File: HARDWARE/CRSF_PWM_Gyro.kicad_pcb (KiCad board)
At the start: 4 copper layers, 32.5 x 22 mm, 27 parts, among them J1 USB_C_Receptacle_USB2.0_16P, J2 Conn_01x21, SW1 SW_SPST, U1 TCR2EF33_LMCT, U2 STM32G431KBTx, Y1 Crystal_GND24

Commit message: Clean up routing and layout
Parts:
- moved C12 2.01 mm to (130.2, 82.6), turned to 0 degrees
- moved R3 2.01 mm to (130.2, 83.8), turned to 180 degrees
- moved R1 1.93 mm to (143.5, 98.3)
- moved R2 1.93 mm to (143.5, 97.1)
- moved R5 1.10 mm to (149.8, 83.1)
- moved C4 0.90 mm to (144.3, 78.7)
- moved LED1 0.40 mm to (147.5, 96.2)
- moved R4 0.30 mm to (150.5, 96.2)
- moved C10 0.10 mm to (130.2, 84.9)
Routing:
- net GND: track 10.1 -> 23.8 mm, vias 26 -> 24
- net Net-(SW1-A): track 15.2 -> 26.9 mm
- net CH4_PWM: track 10.4 -> 7.67 mm
- net +3.3V: track 21.3 -> 23.9 mm, vias 10 -> 9
- net CH3_PWM: track 10.2 -> 7.61 mm
- net CH5_PWM: track 10.9 -> 8.39 mm
- net N_RESET: track 20.7 -> 23.2 mm, vias 2 -> 3
- net CH6_PWM: track 13.1 -> 10.7 mm
- net V_ESC: track 7.83 -> 5.46 mm
- net Net-(J1-CC2): track 23.5 -> 21.5 mm
- net Net-(J1-CC1): track 22.5 -> 20.5 mm
- net Net-(D1-A-Pad2): track 36.4 -> 38.2 mm
- net CH2_PWM: track 13.4 -> 15.2 mm
- net Net-(MT1-AP_SDA/AP_SDIO/AP_SDI): track 10.6 -> 11.9 mm
- net Net-(MT1-AP_SDO/AP_AD0): track 7.95 -> 9.17 mm
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
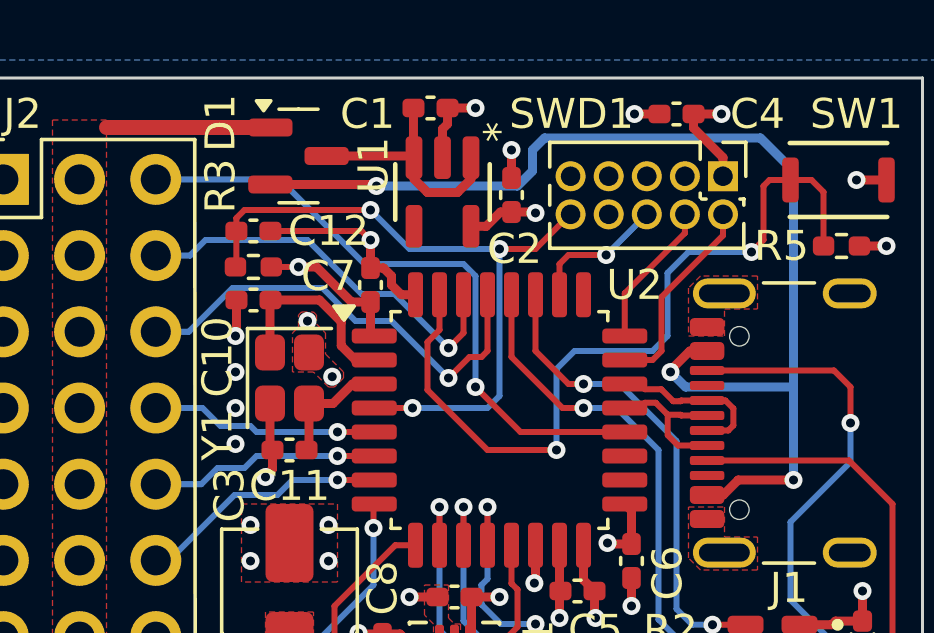
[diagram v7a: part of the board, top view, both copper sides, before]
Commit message: Move some silkscreen text
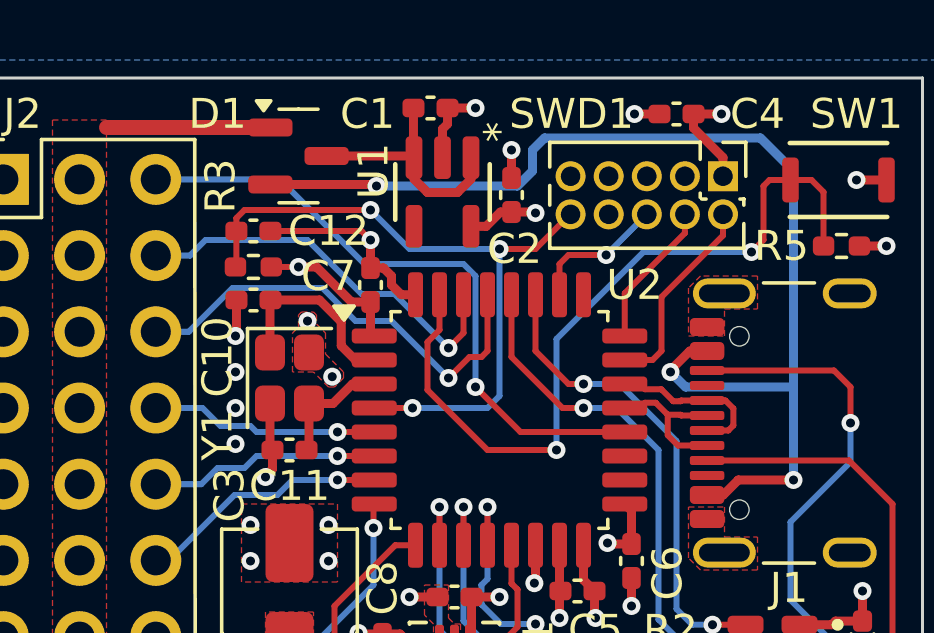
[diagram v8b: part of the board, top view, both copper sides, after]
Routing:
- net Net-(SW1-A): track 26.9 -> 26.3 mm
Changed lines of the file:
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@@
 		(tags "TCR2EF33_LMCT ")
 		(property "Reference" "U1"
-			(at -0.9 2.3 90)
+			(at -0.7 2.3 90)
 			(unlocked yes)
 			(layer "F.SilkS")
@@
 		(tags "SOT TO_SOT_SMD")
 		(property "Reference" "D1"
-			(at -2.6 -1.1 90)
+			(at -2.7 -1.4 180)
 			(layer "F.SilkS")
 			(effects
@@
 	)
 	(gr_text "CH6"
-		(at 128.5 96.1 0)
+		(at 128 96.1 0)
 		(layer "B.SilkS")
 		(effects
@@
 	)
 	(gr_text "CH5"
-		(at 128.5 93.6 0)
+		(at 128 93.6 0)
 		(layer "B.SilkS")
 		(effects
@@
 	)
 	(gr_text "CH3"
-		(at 128.6 88.5 0)
+		(at 128.1 88.5 0)
 		(layer "B.SilkS")
 		(effects
@@
 	)
 	(gr_text "CH1"
-		(at 128.6 83.4 0)
+		(at 128.1 83.4 0)
 		(layer "B.SilkS")
 		(effects
@@
 	)
 	(gr_text "CH4"
-		(at 128.6 91.1 0)
+		(at 128.1 91.1 0)
 		(layer "B.SilkS")
 		(effects
@@
 	)
 	(gr_text "SER"
-		(at 128.7 80.9 0)
+		(at 128.2 80.9 0)
 		(layer "B.SilkS")
 		(effects
@@
 	)
 	(gr_text "CH2"
-		(at 128.6 86 0)
+		(at 128.1 86 0)
 		(layer "B.SilkS")
 		(effects
@@
 	(segment
 		(start 140.3 89.9)
-		(end 140.3 87.2)
+		(end 140.3 86.2)
 		(width 0.2)
 		(layer "B.Cu")
@@
 	)
 	(segment
-		(start 140.9 86.6)
-		(end 143.5 86.6)
+		(start 140.3 86.2)
+		(end 143.2 83.3)
 		(width 0.2)
 		(layer "B.Cu")
@@
 	)
 	(segment
-		(start 140.3 87.2)
-		(end 140.9 86.6)
-		(width 0.2)
-		(layer "B.Cu")
-		(net 27)
-	)
-	(segment
-		(start 144 84)
-		(end 144.7 83.3)
-		(width 0.2)
-		(layer "B.Cu")
-		(net 27)
-	)
-	(segment
-		(start 144.7 83.3)
+		(start 143.2 83.3)
 		(end 146.8 83.3)
 		(width 0.2)
 		(layer "B.Cu")
-		(net 27)
-	)
-	(segment
-		(start 144 86.1)
-		(end 144 84)
-		(width 0.2)
-		(layer "B.Cu")
-		(net 27)
-	)
-	(segment
-		(start 143.5 86.6)
-		(end 144 86.1)
-		(width 0.2)
-		(layer "B.Cu")
